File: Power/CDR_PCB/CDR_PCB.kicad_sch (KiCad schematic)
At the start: 16 parts, among them IC1 TEENSY_4.1, J1 +5V, J2 +3V3, U1 INA226, U2 BNO055, U3 DPS310XTSA1, U4 GNSS

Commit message: Finalised PCB Schematic with missing components
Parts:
- added C3: 470uF, Capacitor_THT:CP_Radial_D8.0mm_P3.50mm, symbol Device:C
- added J3: Transceiver Header, Connector_PinHeader_2.54mm:PinHeader_1x05_P2.54mm_Vertical, symbol Connector_Generic_MountingPin:Conn_02x10_Counter_Clockwise_MountingPin
- added J4: +24V, Connector_PinHeader_2.54mm:PinHeader_1x01_P2.54mm_Vertical, symbol Connector:Screw_Terminal_01x01
- added J5: +14Vin, Connector_PinHeader_2.54mm:PinHeader_1x01_P2.54mm_Vertical, symbol Connector:Screw_Terminal_01x01
- added J6: +14Vout, Connector_PinHeader_2.54mm:PinHeader_1x01_P2.54mm_Vertical, symbol Connector:Screw_Terminal_01x01
- added J7: MOTOR2, Connector_PinHeader_2.54mm:PinHeader_1x01_P2.54mm_Vertical, symbol Connector:Screw_Terminal_01x01
- added J8: MOTOR1, Connector_PinHeader_2.54mm:PinHeader_1x01_P2.54mm_Vertical, symbol Connector:Screw_Terminal_01x01
- added R4: 10K, Resistor_THT:R_Axial_DIN0207_L6.3mm_D2.5mm_P7.62mm_Horizontal, symbol Device:R
- added TP3, TP4: TestPoint, TestPoint:TestPoint_Loop_D2.50mm_Drill1.0mm, symbol Connector:TestPoint
- added U5: DRV8871, Package_SO:Texas_HTSOP-8-1EP_3.9x4.9mm_P1.27mm_EP2.95x4.9mm_Mask2.4x3.1mm_ThermalVias, symbol Driver_Motor:DRV8871DDA
- BT1: footprint (none) -> Battery:BatteryHolder_Multicomp_BC-2001_1x2032
- U2: footprint 2472:MODULE_2472 -> BNO055:MODULE_2472
- U4: footprint 746:XCVR_746 -> GNSS:XCVR_746
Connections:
- net +3V3: now also J3.1 (Pin_1), R4.2
- net +5V: now also C1.1, J1.1 (Pin_1), TP1.1; no longer U1.9 (Vin-)
- net GND: now also C3.2, J3.10 (Pin_10), U5.1 (GND), U5.7 (GND), U5.9 (GND)
- net DRV_IN1: now reaches IC1.20 (A6)
- net DRV_IN1: now also U5.3 (IN1)
- net DRV_IN2: now reaches IC1.21 (A7)
- net DRV_IN2: now also U5.2 (IN2)
- net XB_RESET: now reaches IC1.22 (A8)
- net XB_RESET: now also J3.5 (Pin_5), R4.1
- net RX2: now reaches IC1.7 (RX2)
- net RX2: now also J3.2 (Pin_2)
- net TX2: now reaches IC1.8 (TX2)
- net TX2: now also J3.3 (Pin_3)
- net RX renamed RX1
- net TX renamed TX1
- new net: J5.1 (Pin_1), TP4.1, U1.10 (Vin+), U1.8 (Vbus)
- new net: J6.1 (Pin_1), U1.9 (Vin-)
- new net: J8.1 (Pin_1), U5.6 (OUT1)
- new net: J7.1 (Pin_1), U5.8 (OUT2)
- new net +24V: C3.1, J4.1 (Pin_1), TP3.1, U5.5 (VM)
- no-connect marks 3 -> 19
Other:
- note added: "Electrical Power System (EPS) & Monitoring"
- note added: "Motor Driver"
- note added: "Telemetry"
- note removed: "Electrical Power System & Monitoring"
- moved on the sheet: BT1, C1, C2, D1, IC1, J1, J2, R3, TP1, TP2, U1, U3

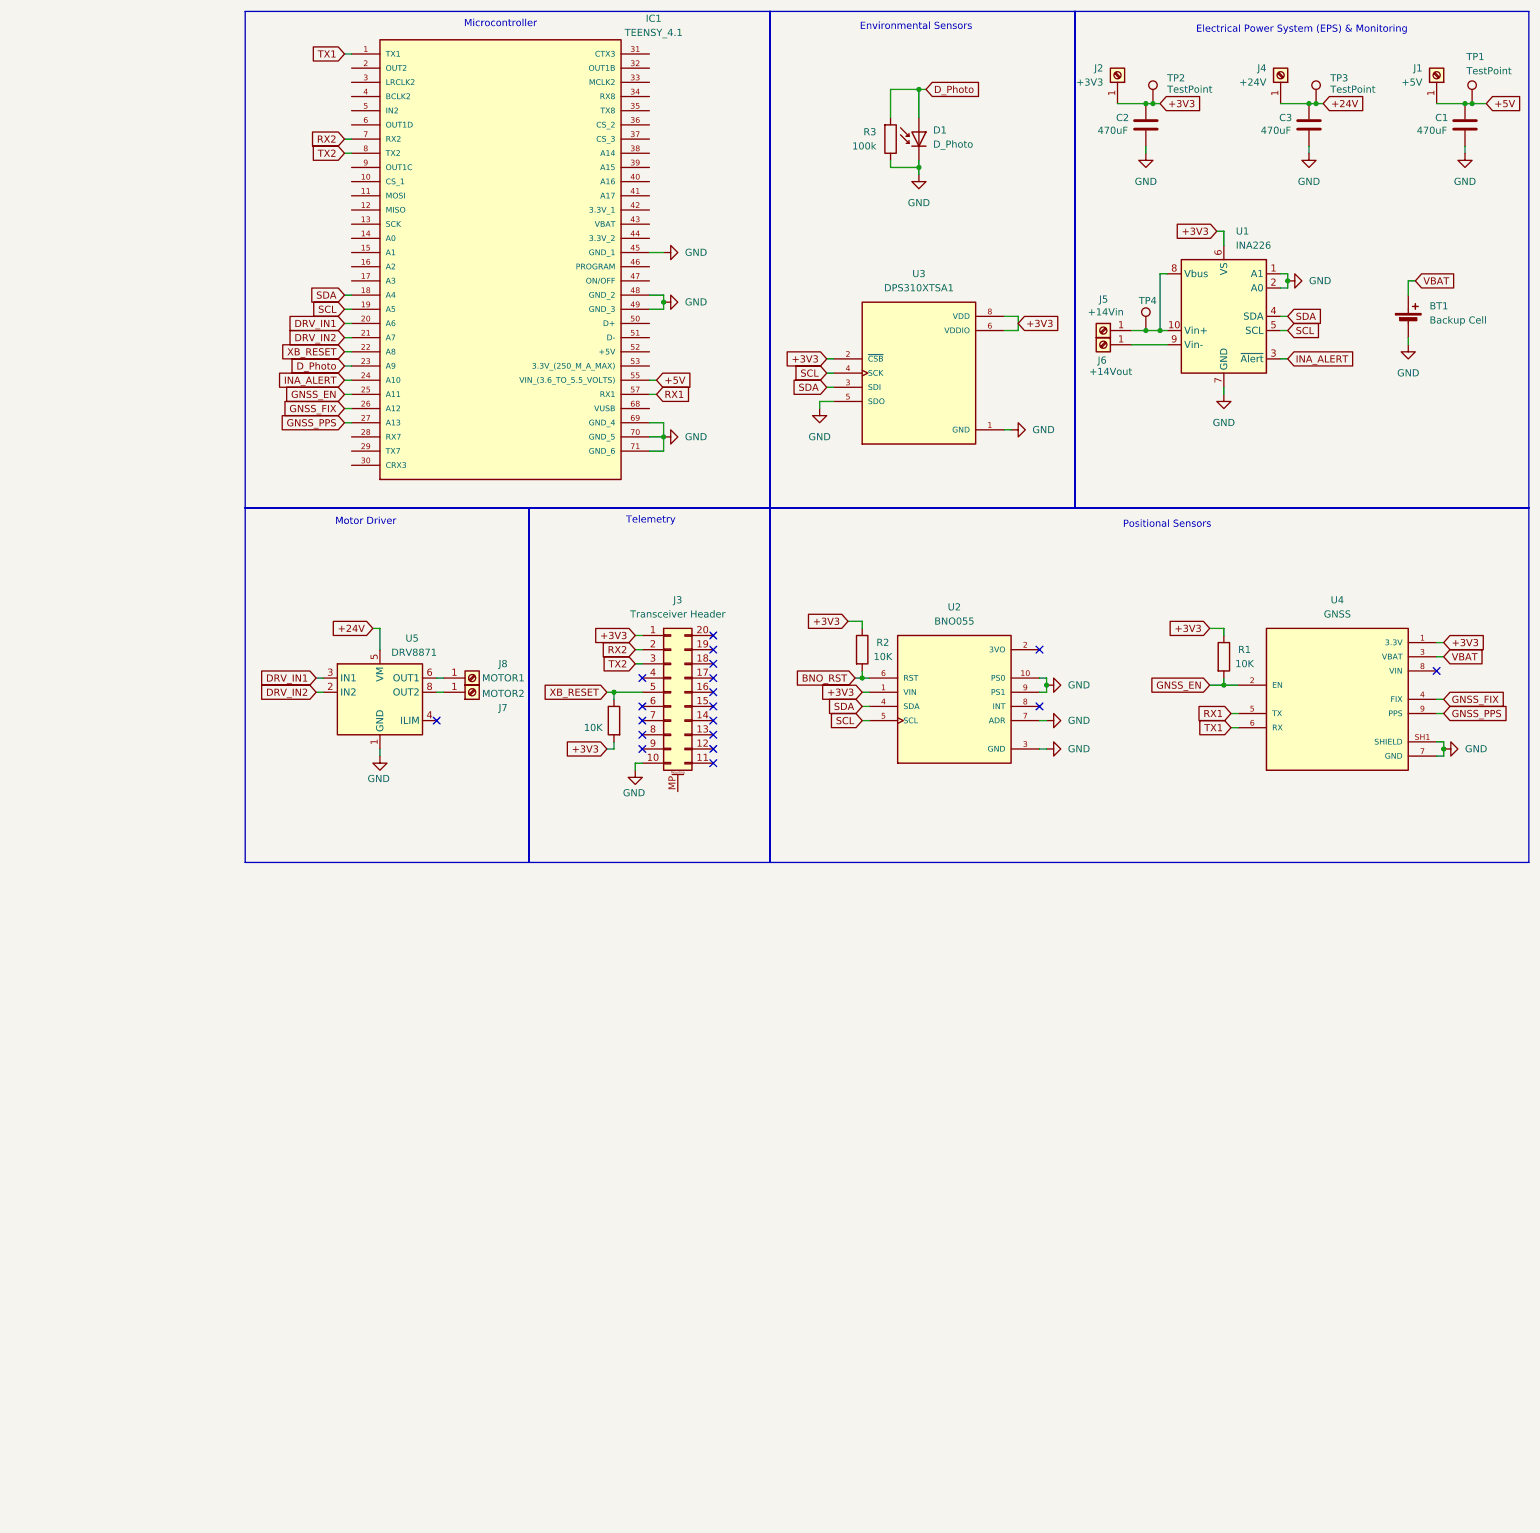
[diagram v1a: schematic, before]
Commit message: Adjusted photodiodes & added missing components
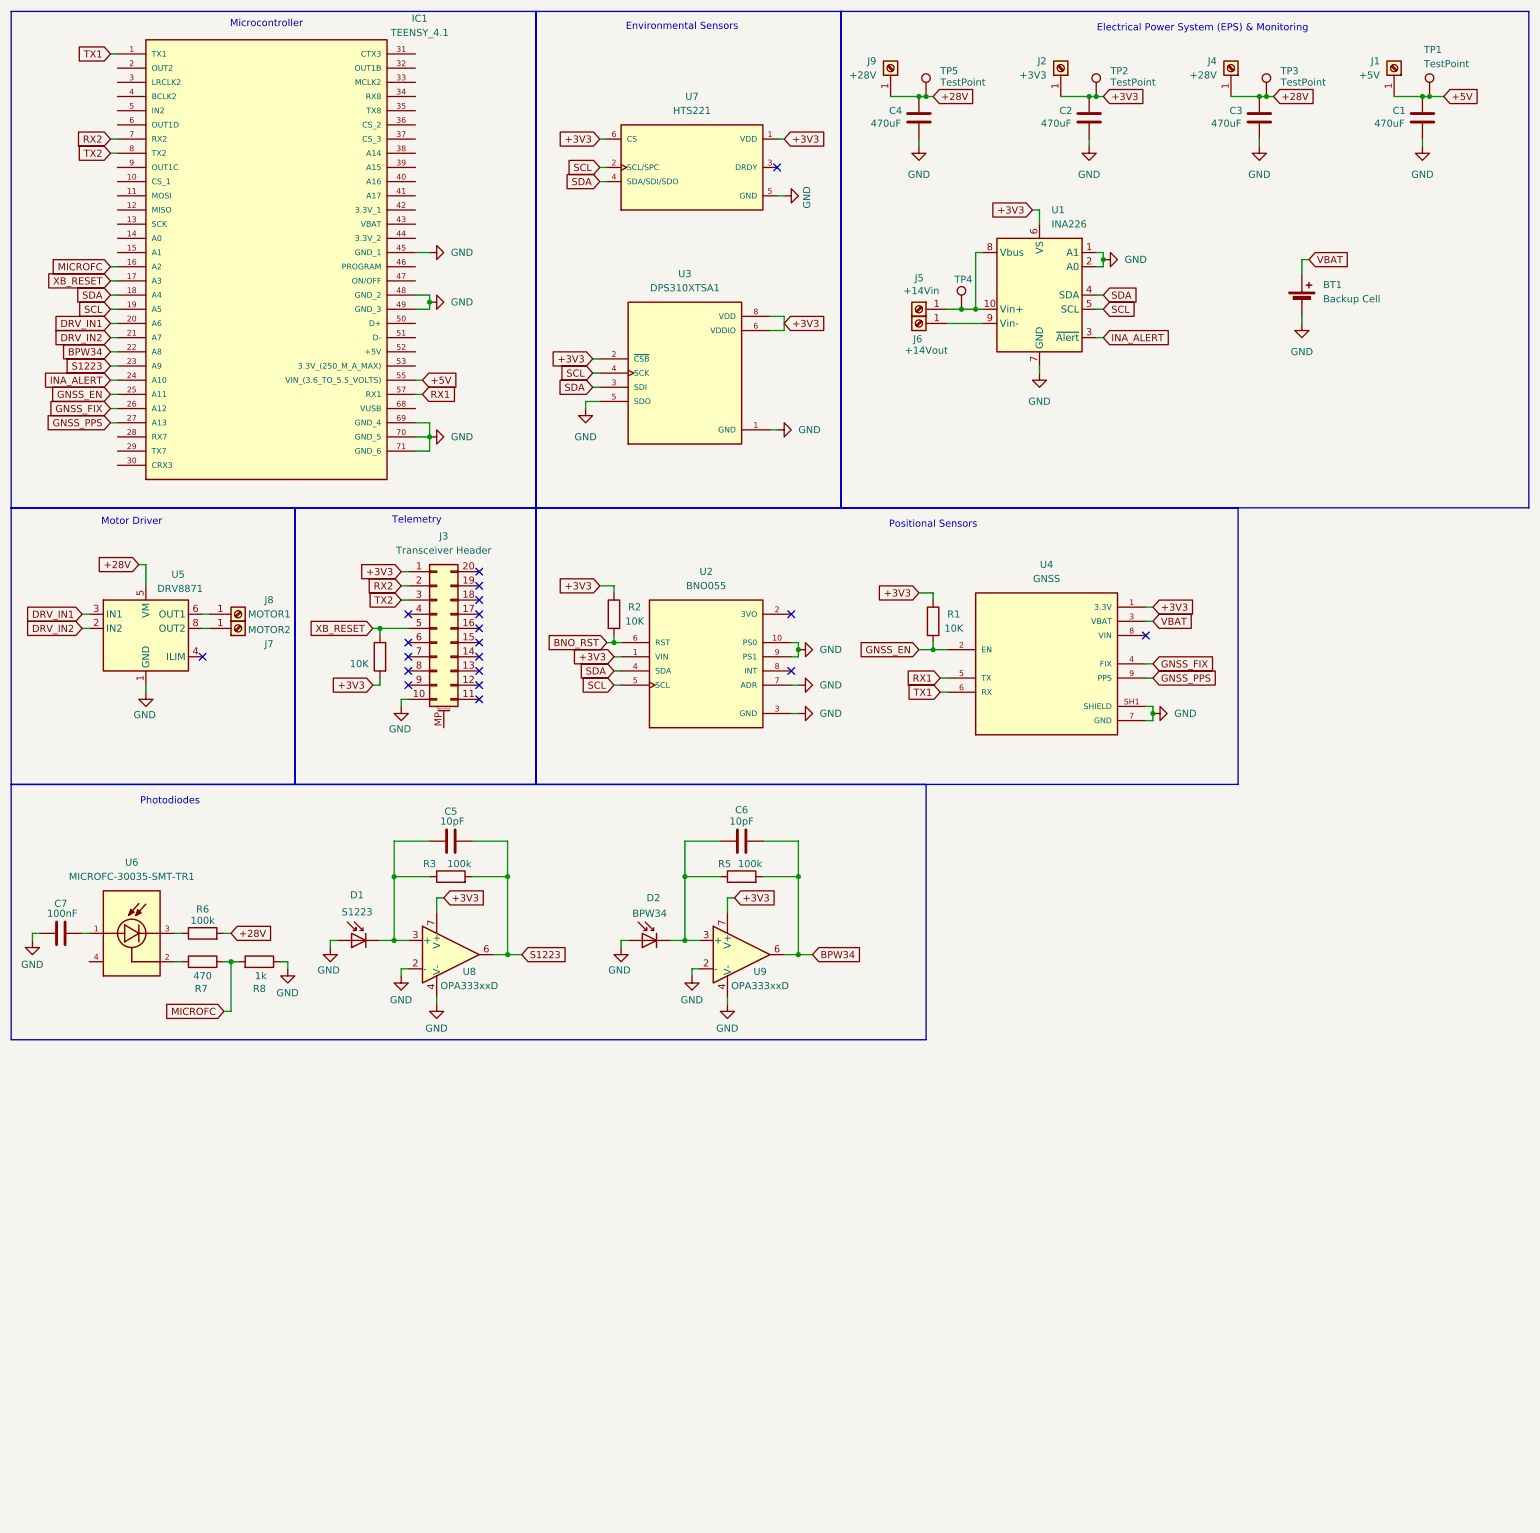
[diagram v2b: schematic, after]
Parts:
- added C4: 470uF, Capacitor_THT:CP_Radial_D8.0mm_P3.50mm, symbol Device:C
- added C5, C6: 10pF, symbol Device:C
- added C7: 100nF, symbol Device:C
- added D2: BPW34, Diode_THT:D_DO-35_SOD27_P3.81mm_Vertical_AnodeUp, symbol Device:D_Photo
- added J9: +28V, Connector_PinHeader_2.54mm:PinHeader_1x01_P2.54mm_Vertical, symbol Connector:Screw_Terminal_01x01
- added R5, R6: 100k, symbol Device:R
- added R7: 470, symbol Device:R
- added R8: 1k, symbol Device:R
- added TP5: TestPoint, TestPoint:TestPoint_Loop_D2.50mm_Drill1.0mm, symbol Connector:TestPoint
- added U6: MICROFC-30035-SMT-TR1, MICROFC-30035-SMT-TR1:XDCR_MICROFC-30035-SMT-TR1, symbol MICROFC-30035-SMT-TR1:MICROFC-30035-SMT-TR1
- added U7: HTS221, HTS221:XDCR_HTS221, symbol HTS221:HTS221
- added U8, U9: OPA333xxD, Package_SO:SOIC-8_3.9x4.9mm_P1.27mm, symbol Amplifier_Operational:OPA333xxD
- D1: value D_Photo -> S1223
- J4: value +24V -> +28V
- R3: footprint Resistor_THT:R_Axial_DIN0207_L6.3mm_D2.5mm_P7.62mm_Horizontal -> (none)
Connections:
- net +3V3: now also U7.1 (VDD), U7.6 (CS), U8.7 (V+), U9.7 (V+)
- net GND: now also D1.2 (A), C4.2, C7.2, D2.2 (A), R8.1, U7.5 (GND), U8.2 (-), U8.4 (V-), U9.2 (-), U9.4 (V-); no longer D1.1 (K), R3.1
- net SCL: now also U7.2 (SCL/SPC)
- net SDA: now also U7.4 (SDA/SDI/SDO)
- net XB_RESET: now also IC1.17 (A3); no longer IC1.22 (A8)
- net MICROFC: now reaches IC1.16 (A2)
- net MICROFC: now also R7.1, R8.2
- net +24V renamed +28V
- net +28V: now also C4.1, J9.1 (Pin_1), R6.2, TP5.1
- net D_Photo renamed S1223
- net S1223: now also C5.1, U8.6; no longer D1.2 (A)
- new net: C6.2, D2.1 (K), R5.1, U9.3 (+)
- new net: C5.2, D1.1 (K), R3.1, U8.3 (+)
- new net: R6.1, U6.3
- new net: C7.1, U6.1
- new net: R7.2, U6.2
- new net BPW34: C6.1, IC1.22 (A8), R5.2, U9.6
- no-connect marks 19 -> 20
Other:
- note added: "Photodiodes"
- moved on the sheet: BT1, C1, C2, C3, D1, IC1, J1, J2, J3, J4, J5, J6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

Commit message: Minor EPS changes
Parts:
- added D3: D, symbol Device:D
- J9: value +28V -> +24V
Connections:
- net +28V: no longer C4.1, J9.1 (Pin_1), TP5.1, U5.5 (VM)
- net GND: now also D3.1 (K); no longer BT1.2 (-)
- new net: BT1.2 (-), D3.2 (A)
- new net +24V: C4.1, J9.1 (Pin_1), TP5.1, U5.5 (VM)
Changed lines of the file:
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@@
 	(wire
 		(pts
+			(xy 243.84 76.2) (xy 243.84 77.47)
+		)
+		(stroke
+			(width 0)
+			(type default)
+		)
+	)
+	(wire
+		(pts
 			(xy 170.18 27.94) (xy 175.26 27.94)
 		)
@@
 		)
 	)
-	(global_label "+28V"
+	(global_label "+24V"
 		(shape input)
 		(at 177.8 27.94 0)
@@
 		)
 	)
-	(global_label "+28V"
+	(global_label "+24V"
 		(shape input)
 		(at 35.56 111.76 180)
@@
 	)
 	(symbol
+		(lib_id "Device:D")
+		(at 243.84 72.39 90)
+		(unit 1)
+		(exclude_from_sim no)
+		(in_bom yes)
+		(on_board yes)
+		(dnp no)
+		(fields_autoplaced yes)
+		(property "Reference" "D3"
+			(at 246.38 71.1199 90)
+			(effects
+				(font
+					(size 1.27 1.27)
+				)
+				(justify right)
+			)
+		)
+		(property "Value" "D"
+			(at 246.38 73.6599 90)
+			(effects
+				(font
+					(size 1.27 1.27)
+				)
+				(justify right)
+			)
+		)
+		(property "Footprint" ""
+			(at 243.84 72.39 0)
+			(effects
+				(font
+					(size 1.27 1.27)
+				)
+				(hide yes)
+			)
+		)
+		(property "Datasheet" "~"
+			(at 243.84 72.39 0)
+			(effects
+				(font
+					(size 1.27 1.27)
+				)
+				(hide yes)
+			)
+		)
+		(property "Description" "Diode"
+			(at 243.84 72.39 0)
+			(effects
+				(font
+					(size 1.27 1.27)
+				)
+				(hide yes)
+			)
+		)
+		(property "Sim.Device" "D"
+			(at 243.84 72.39 0)
+			(effects
+				(font
+					(size 1.27 1.27)
+				)
+				(hide yes)
+			)
+		)
+		(property "Sim.Pins" "1=K 2=A"
+			(at 243.84 72.39 0)
+			(effects
+				(font
+					(size 1.27 1.27)
+				)
+				(hide yes)
+			)
+		)
+		(pin "2"
+		)
+		(pin "1"
+		)
+		(instances
+			(project "CDR_PCB"
+				(path "/999c58ce-3f2b-445b-83c5-b596e3f1e757"
+					(reference "D3")
+					(unit 1)
+				)
+			)
+		)
+	)
+	(symbol
 		(lib_id "power:GND")
 		(at 82.55 137.16 0)
@@
 			)
 		)
-		(property "Value" "+28V"
+		(property "Value" "+24V"
 			(at 167.64 24.1299 90)
 			(effects
@@
 	(symbol
 		(lib_id "power:GND")
-		(at 243.84 68.58 0)
+		(at 243.84 77.47 0)
 		(unit 1)
 		(exclude_from_sim no)
@@
 		(fields_autoplaced yes)
 		(property "Reference" "#PWR09"
-			(at 243.84 74.93 0)
+			(at 243.84 83.82 0)
 			(effects
 				(font
@@
 		)
 		(property "Value" "GND"
-			(at 243.84 73.66 0)
+			(at 243.84 82.55 0)
 			(effects
 				(font
@@
 		)
 		(property "Footprint" ""
-			(at 243.84 68.58 0)
+			(at 243.84 77.47 0)
 			(effects
 				(font
@@
 		)
 		(property "Datasheet" ""
-			(at 243.84 68.58 0)
+			(at 243.84 77.47 0)
 			(effects
 				(font
@@
 		)
 		(property "Description" "Power symbol creates a global label with name \"GND\" , ground"
-			(at 243.84 68.58 0)
+			(at 243.84 77.47 0)
 			(effects
 				(font

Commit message: Wed 04/03
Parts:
- added R9: TBD, Resistor_THT:R_Axial_DIN0207_L6.3mm_D2.5mm_P7.62mm_Horizontal, symbol Device:R
- C1, C2, C3, C4: symbol Device:C -> Device:C_Polarized
- C5, C6, C7: footprint (none) -> Capacitor_THT:C_Disc_D3.0mm_W1.6mm_P2.50mm
- D3: footprint (none) -> Diode_THT:D_DO-15_P10.16mm_Horizontal
- R3, R5, R6, R7, R8: footprint (none) -> Resistor_THT:R_Axial_DIN0207_L6.3mm_D2.5mm_P7.62mm_Horizontal
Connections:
- net +24V: no longer U5.5 (VM)
- net +28V: now also R9.1
- net GND: now also U8.3 (+), U9.3 (+); no longer U8.2 (-), U9.2 (-)
- net at C6.2, D2.1 (K), R5.1: now also U9.2 (-); no longer U9.3 (+)
- net at C5.2, D1.1 (K), R3.1: now also U8.2 (-); no longer U8.3 (+)
- new net: R9.2, U5.5 (VM)
- no-connect marks 20 -> 57
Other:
- moved on the sheet: D1, D2

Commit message: Updated PCB
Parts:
- removed C4: 470uF, Capacitor_THT:CP_Radial_D8.0mm_P3.50mm, symbol Device:C_Polarized
- removed J3: Transceiver Header, Connector_PinHeader_2.54mm:PinHeader_1x05_P2.54mm_Vertical, symbol Connector_Generic_MountingPin:Conn_02x10_Counter_Clockwise_MountingPin
- removed J9: +24V, Connector_PinHeader_2.54mm:PinHeader_1x01_P2.54mm_Vertical, symbol Connector:Screw_Terminal_01x01
- removed TP5: TestPoint, TestPoint:TestPoint_Loop_D2.50mm_Drill1.0mm, symbol Connector:TestPoint
- added D10, D11, D4, D5, D6, D7, D8, D9: LED, LED_THT:LED_D3.0mm, symbol Device:LED
- added J10: Transceiver header, Connector_PinHeader_2.54mm:PinHeader_1x05_P2.54mm_Vertical, symbol Connector_Generic:Conn_01x05
- added J3: Lower_PCB_Header, symbol Connector_Generic:Conn_02x25_Top_Bottom
- added J9: Converter_GND_Lines, Connector_PinHeader_2.54mm:PinHeader_1x03_P2.54mm_Vertical, symbol Connector:Screw_Terminal_01x04
- added R10, R12: 10K, Resistor_THT:R_Axial_DIN0207_L6.3mm_D2.5mm_P7.62mm_Horizontal, symbol Device:R
- added R11: 1K, Resistor_THT:R_Axial_DIN0207_L6.3mm_D2.5mm_P7.62mm_Horizontal, symbol Device:R
- added R13, R14, R15, R16, R17: 470, Resistor_THT:R_Axial_DIN0207_L6.3mm_D2.5mm_P7.62mm_Horizontal, symbol Device:R
- D1, D2: footprint Diode_THT:D_DO-35_SOD27_P3.81mm_Vertical_AnodeUp -> Connector_PinHeader_2.54mm:PinHeader_1x02_P2.54mm_Horizontal
- J6: footprint Connector_PinHeader_2.54mm:PinHeader_1x01_P2.54mm_Vertical -> Connector_PinHeader_2.54mm:PinHeader_1x03_P2.54mm_Vertical; symbol Connector:Screw_Terminal_01x01 -> Connector:Screw_Terminal_01x03
- R4: value 10K -> 330
- U5: footprint Package_SO:Texas_HTSOP-8-1EP_3.9x4.9mm_P1.27mm_EP2.95x4.9mm_Mask2.4x3.1mm_ThermalVias -> Library_motordriver:DRV8871 BOARD
- U6: footprint MICROFC-30035-SMT-TR1:XDCR_MICROFC-30035-SMT-TR1 -> Connector_PinHeader_2.54mm:PinHeader_1x04_P2.54mm_Vertical
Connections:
- net +28V: now also C1.1, J1.1 (Pin_1), TP1.1, D6.2 (A), J3.1 (Pin_1), J3.2 (Pin_2); no longer C3.1, J4.1 (Pin_1), TP3.1
- net +3V3: now also D4.2 (A), J10.1 (Pin_1), J3.5 (Pin_5), R10.2; no longer R4.2
- net +5V: now also C3.1, J4.1 (Pin_1), TP3.1, D5.2 (A), J3.6 (Pin_6); no longer C1.1, J1.1 (Pin_1), TP1.1
- net DRV_IN1: now also J3.11 (Pin_11)
- net DRV_IN2: now also J3.12 (Pin_12)
- net GND: now also R4.2, J10.5 (Pin_5), J3.3 (Pin_3), J3.4 (Pin_4), J3.7 (Pin_7), J3.8 (Pin_8), J9.1 (Pin_1), J9.2 (Pin_2), J9.3 (Pin_3), J9.4 (Pin_4), R11.2, R12.2, R13.2, R14.2, R15.2, R16.2, R17.2
- net RX1: now also D8.2 (A)
- net RX2: now also D10.2 (A), J10.2 (Pin_2)
- net SCL: now also J3.10 (Pin_10)
- net SDA: now also J3.9 (Pin_9)
- net TX1: now also D9.2 (A)
- net TX2: now also D11.2 (A), J10.3 (Pin_3)
- net XB_RESET: now also J10.4 (Pin_4), J3.13 (Pin_13), R10.1; no longer R4.1
- net at J6.1 (Pin_1), U1.9 (Vin-): now also J6.2 (Pin_2), J6.3 (Pin_3)
- net Status_LED: now reaches IC1.15 (A1)
- net Status_LED: now also D7.2 (A)
- new net: D4.1 (K), R4.1
- new net: D7.1 (K), R13.1
- new net: D8.1 (K), R14.1
- new net: D9.1 (K), R15.1
- new net: D10.1 (K), R16.1
- new net: D5.1 (K), R11.1
- new net: D6.1 (K), R12.1
- new net: D11.1 (K), R17.1
- no-connect marks 57 -> 41
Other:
- note added: "Debugging LEDs"
- note added: "EPS Monitoring"
- note added: "Electrical Power System (EPS)"
- note added: "Multi-PCB Headers"
- note removed: "Electrical Power System (EPS) & Monitoring"
- company: (none) -> Project Sunsat - HYPERIONyX Mission 2025/26
- title: (none) -> Project HYPERIONyX CDR PCB
- moved on the sheet: BT1, C1, C2, C3, D1, D2, D3, J1, J2, J4, J5, R1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
